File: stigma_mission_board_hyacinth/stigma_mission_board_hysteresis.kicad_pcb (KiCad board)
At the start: 4 copper layers, 70 x 110 mm, 269 parts, among them J10 Conn_02x05_Top_Bottom_Mountin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, J13 SMA, J16 Conn_02x02_Top_Bottom, J17 Conn_02x02_Top_Bottom, J18 Conn_02x02_Top_Bottom, J19 Conn_02x02_Top_Bottom, J2 SMA, J3 Conn_02x04_Top_Bottom, J5 Conn_02x02_Top_Bottom, J6 JST-GH, J8 Conn_02x04_Top_Bottom, Q1 DMN2056U, Q10 DMN2056U, Q11 AOSP21321, Q14 DMN2056U, Q15 AOSP21321, Q2 DMN2056U, Q3 AOSP21321, Q6 DMN2056U, Q7 AOSP21321, U1 L7805, U10 Ai-Thinker-Ra-01, U10 INA181, U11 INA181, U12 LAN8742A, U13 TPD4E1U06, U14 INA181, U16 INA181, U17 Ai-Thinker-Ra-01, U2 L7805, U3 Ai-Thinker-Ra-01, U3 L7805, U4 SN74HCS594, U5 MCP2562-E-SN, U6 MCP2562-E-SN, U7 AZ1117H-ADJ, U8 AZ1117H-ADJ, U9 INA181, Y1 25MHz

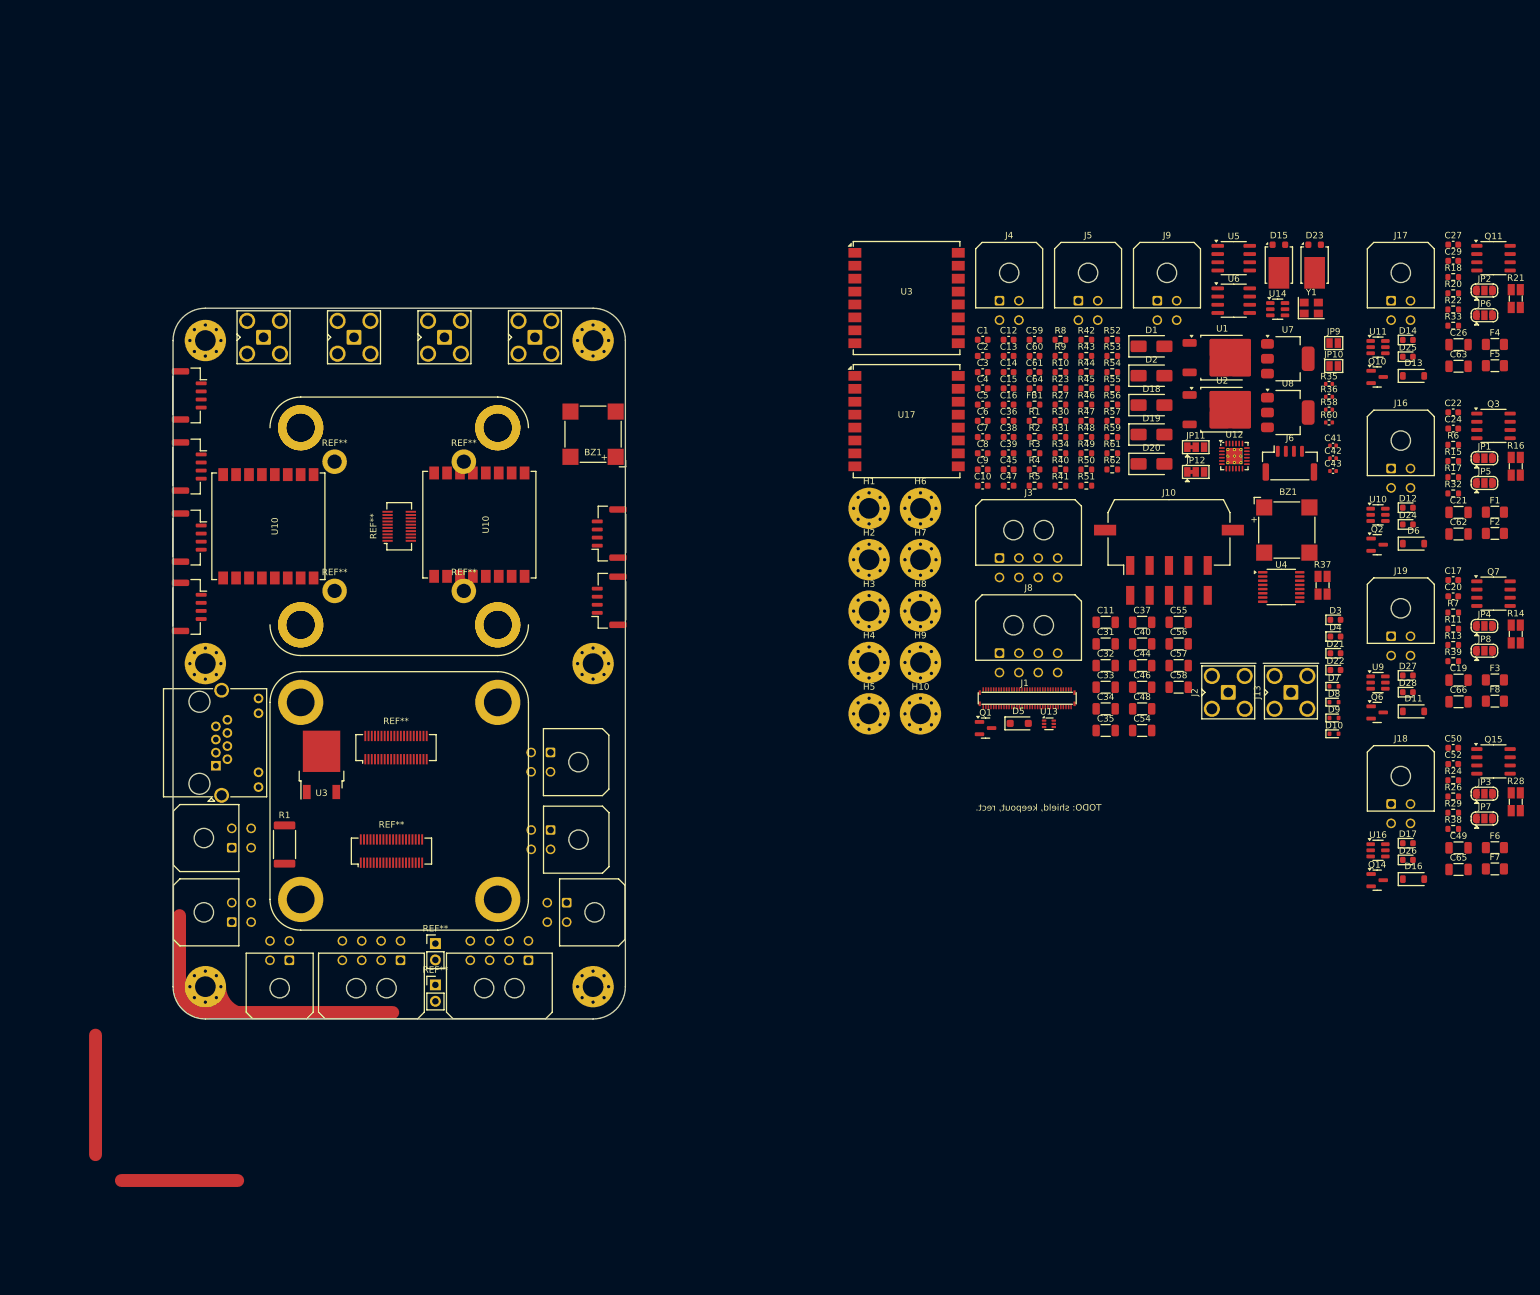
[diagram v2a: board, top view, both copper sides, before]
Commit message: changed pcb layout and added first tracks
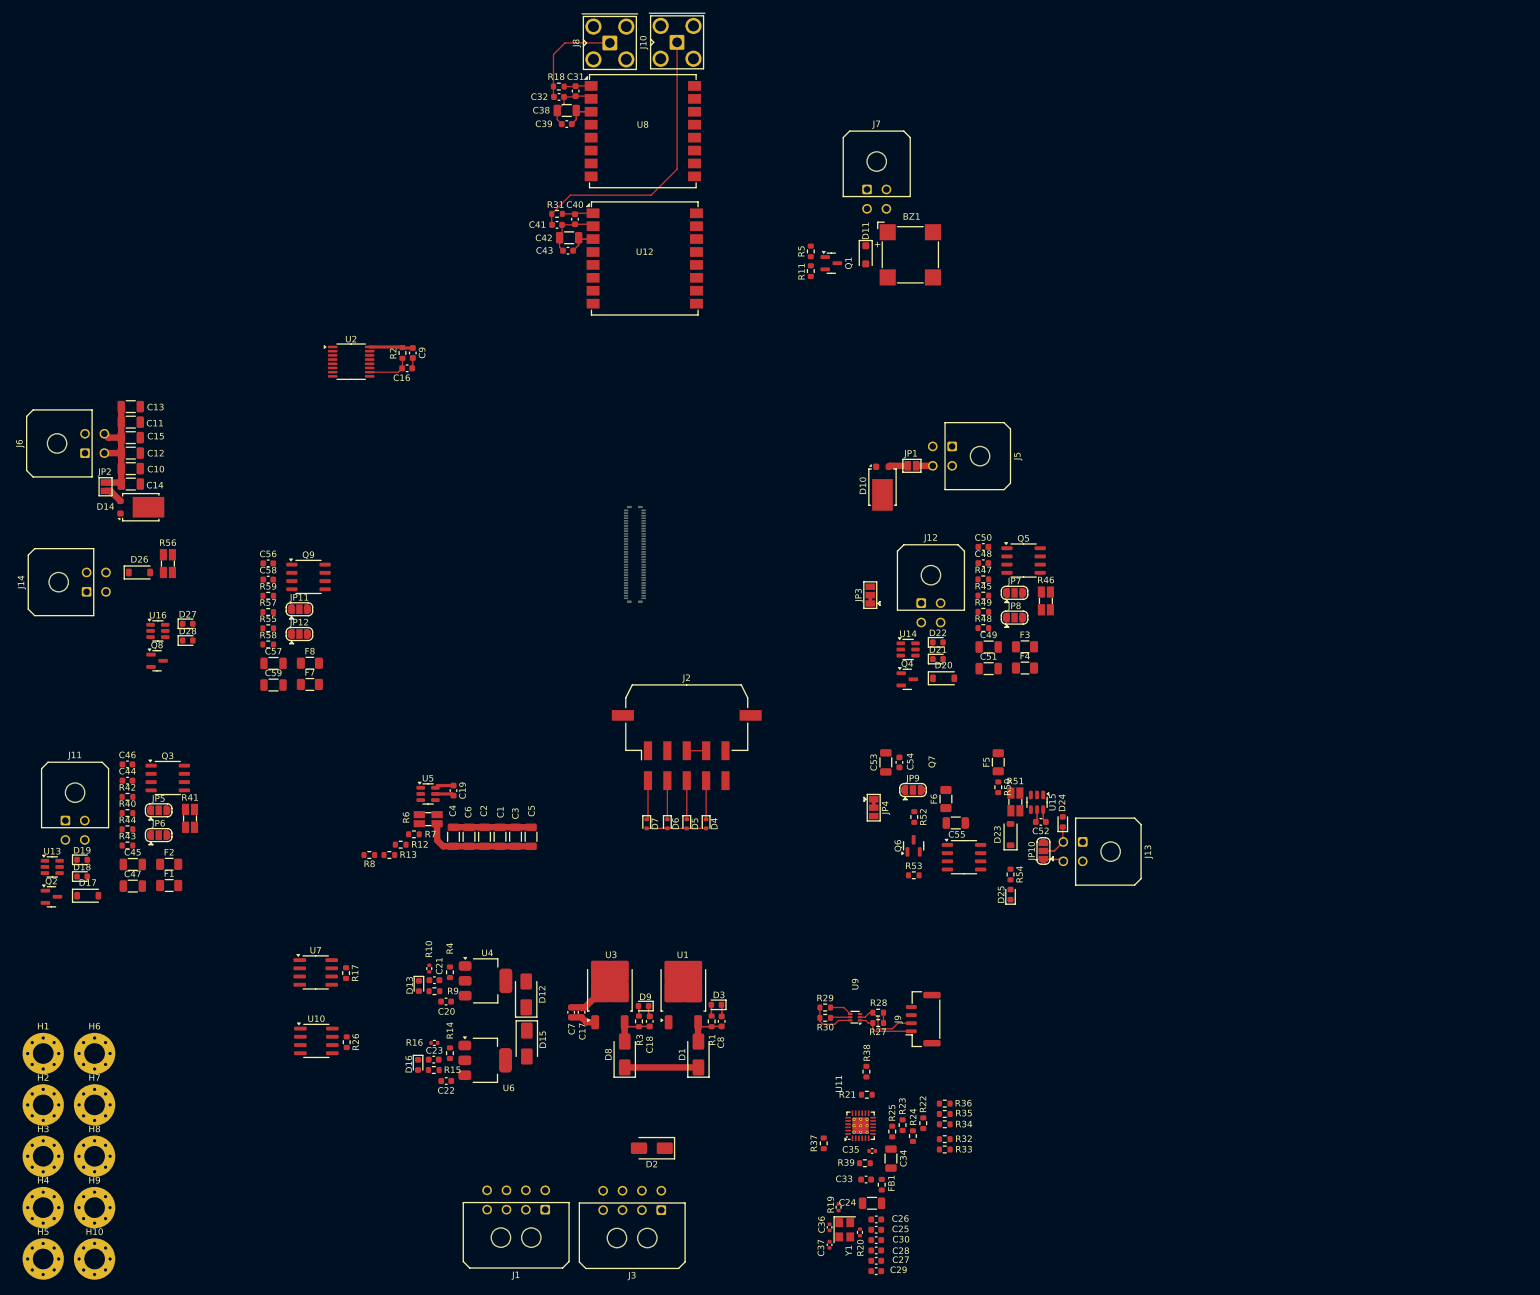
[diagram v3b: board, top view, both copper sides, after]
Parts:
- removed the BZ1 at (105.0, 64.5)
- removed the R1 at (57.2, 128.0)
- removed REF** (x2): Molex_Micro-Fit_3.0_43045-0800_2x04_P3.00mm_Horizontal, Connector_Molex:Molex_Micro-Fit_3.0_43045-0800_2x04_P3.00mm_Horizontal
- removed REF** (x12): MountingHole_4.3mm_M4_ISO14580_Pad, MountingHole:MountingHole_4.3mm_M4_ISO14580_Pad
- removed REF** (x4): SMA_Amphenol_901-143_Horizontal, Connector_Coaxial:SMA_Amphenol_901-143_Horizontal
- removed REF** (x6): JST_GH_SM04B-GHS-TB_1x04-1MP_P1.25mm_Horizontal, Connector_JST:JST_GH_SM04B-GHS-TB_1x04-1MP_P1.25mm_Horizontal
- removed REF** (x6): Molex_Micro-Fit_3.0_43045-0400_2x02_P3.00mm_Horizontal, Connector_Molex:Molex_Micro-Fit_3.0_43045-0400_2x02_P3.00mm_Horizontal
- removed REF** (x4): MountingHole_2.2mm_M2_ISO14580_Pad, MountingHole:MountingHole_2.2mm_M2_ISO14580_Pad
- removed REF** (x6): MountingHole_3.2mm_M3_Pad_Via, MountingHole:MountingHole_3.2mm_M3_Pad_Via
- removed REF**: RJ45_Amphenol_RJHSE538X, Connector_RJ:RJ45_Amphenol_RJHSE538X
- removed REF** (x2): PinHeader_1x02_P2.54mm_Vertical, Connector_PinHeader_2.54mm:PinHeader_1x02_P2.54mm_Vertical
- removed REF** (x2): Hirose_DF12_DF12E3.0-40DP-0.5V_2x20_P0.50mm_Vertical, Connector_Hirose:Hirose_DF12_DF12E3.0-40DP-0.5V_2x20_P0.50mm_Vertical
- removed REF**: Hirose_DF12_DF12C3.0-20DS-0.5V_2x10_P0.50mm_Vertical, Connector_Hirose:Hirose_DF12_DF12C3.0-20DS-0.5V_2x10_P0.50mm_Vertical
- removed the U10 at (54.8, 78.8)
- removed the U10 at (87.4, 78.5)
- removed the U3 at (63.0, 115.7)
- J4: renamed from J1; moved to B.Cu
- moved C44 212.3 mm to (32.9, 118.1)
- moved C45 212.3 mm to (33.8, 131.1)
- moved C46 212.3 mm to (32.9, 115.6)
- moved C47 212.3 mm to (33.8, 134.4)
- moved Q3 212.3 mm to (39.2, 117.7)
- moved R40 212.3 mm to (32.9, 123.1)
- moved R41 212.3 mm to (42.6, 124.0)
- moved R42 212.3 mm to (32.9, 120.6)
- moved R43 212.3 mm to (32.9, 128.2)
- moved R44 212.3 mm to (32.9, 125.6)
- moved D17 212.3 mm to (26.8, 135.9)
- moved D18 212.3 mm to (25.9, 133.0)
- moved D19 212.3 mm to (25.9, 130.4)
- moved F1 212.3 mm to (39.4, 134.3)
- moved F2 212.3 mm to (39.4, 131.1)
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- renumbered C31 to C1, C32 to C10, C34 to C11, C35 to C12, C54 to C13, C56 to C14, C58 to C15, C8 to C16, C2 to C17, C4 to C18, C47 to C19, C33 to C2, C12 to C20, C13 to C21, C14 to C22, C15 to C23, C37 to C24, C38 to C25, C39 to C26, C60 to C27, C61 to C28, C59 to C29, C46 to C3, C36 to C30, C5 to C31, C6 to C32, C64 to C33, C40 to C34, C41 to C35, C42 to C36, C43 to C37, C44 to C38, C45 to C39, C48 to C4, C9 to C40, C10 to C41, C11 to C42, C16 to C43, C24 to C44, C21 to C45, C22 to C46, C62 to C47, C29 to C48, C26 to C49, C55 to C5, C27 to C50, C63 to C51, C49 to C53, C50 to C54, C65 to C55, C17 to C56, C19 to C57, C20 to C58, C66 to C59, C57 to C6, C1 to C7, C3 to C8, C7 to C9, D15 to D10, D5 to D11, D2 to D12, D21 to D13, D23 to D14, D20 to D15, D22 to D16, D6 to D17, D24 to D18, D12 to D19, D19 to D2, D13 to D20, D25 to D21, D14 to D22, D16 to D23, D26 to D24, D17 to D25, D11 to D26, D7 to D4, D8 to D5, D9 to D6, D10 to D7, D18 to D8, D4 to D9, F2 to F1, F1 to F2, F4 to F3, F5 to F4, F6 to F5, F7 to F6, F8 to F7, F3 to F8, J8 to J1, J13 to J10, J16 to J11, J17 to J12, J18 to J13, J19 to J14, J10 to J2, J4 to J5, J9 to J6, J5 to J7, J2 to J8, J6 to J9, JP9 to JP1, JP7 to JP10, JP4 to JP11, JP8 to JP12, JP10 to JP2, JP12 to JP3, JP11 to JP4, JP1 to JP5, JP5 to JP6, JP2 to JP7, JP6 to JP8, JP3 to JP9, Q10 to Q4, Q11 to Q5, Q14 to Q6, Q15 to Q7, Q6 to Q8, Q7 to Q9, R60 to R10, R8 to R11, R27 to R12, R31 to R13, R57 to R14, R62 to R15, R58 to R16, R9 to R17, R3 to R18, R35 to R19, R4 to R2, R36 to R20, R55 to R21, R53 to R22, R48 to R23, R47 to R24, R46 to R25, R10 to R26, R41 to R27, R42 to R28, R43 to R29, R2 to R3, R44 to R30, R5 to R31, R45 to R32, R49 to R33, R50 to R34, R51 to R35, R52 to R36, R34 to R37, R54 to R38, R56 to R39, R59 to R4, R15 to R40, R16 to R41, R6 to R42, R32 to R43, R17 to R44, R20 to R45, R21 to R46, R18 to R47, R33 to R48, R22 to R49, R40 to R5, R26 to R50, R28 to R51, R24 to R52, R38 to R53, R29 to R54, R13 to R55, R14 to R56, R11 to R57, R39 to R58, R7 to R59, R37 to R6, R23 to R7, R30 to R8, R61 to R9, U6 to U10, U12 to U11, U17 to U12, U10 to U13, U11 to U14, U16 to U15, U9 to U16, U4 to U2, U2 to U3, U7 to U4, U14 to U5, U8 to U6, U5 to U7, U3 to U8, U13 to U9
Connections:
- J2 pad MP: unconnected-(J10-MountPin-PadMP) -> GND
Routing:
- net (no net): track 90.2 -> 0.00 mm
- net GND: track 0.00 -> 58.2 mm
- net Net-(J10-In): track 0.00 -> 43.6 mm
- net main_voltage: track 0.00 -> 21.5 mm
- net high_current: track 0.00 -> 20.0 mm
- net Net-(J8-In): track 0.00 -> 16.1 mm
- net +3.3V: track 0.00 -> 11.8 mm
- net +5V: track 0.00 -> 11.4 mm
- net /TXN: track 0.00 -> 10.5 mm
- net +3V3: track 0.00 -> 9.44 mm
- net /TXP: track 0.00 -> 9.19 mm
- net Net-(U11-VDD1A): track 0.00 -> 8.86 mm
- net Net-(U2-~{RCLR}): track 0.00 -> 6.84 mm
- net Net-(D1-A): track 0.00 -> 6.67 mm
- net Net-(D8-A): track 0.00 -> 6.60 mm
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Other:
- board outline removed
- board text added: "3.3V Regulator"
- board text added: "5V Regulator"
- board text added: "@TODO -wohin mit den Teilen, die rechts sind? -Brauchen wir auf dem Board echt Bezeichner + Value, oder reicht Bezeichner? -ist der Connector jetzt falsch rum, weil er blau ist? -Gibt es Teile, die näher am Connector sein MÜSSEN, bzw. bei welchen ist es weniger wichtig? - Über Paint (Bezeichner und so) kann man schon Vias verlegen, oder?"
- board text added: "Buzzer + DAC"
- board text added: "CAN"
- board text added: "Ethernet"
- board text added: "GPS"
- board text added: "LoRa Module"
- board text added: "R1"
- board text added: "R2"
- board text added: "R3"
- board text added: "R4"
- board text added: "Recovery Power 1"
- board text added: "Recovery Power 2"
- board text added: "Shift Register IO"
- board text added: "Vehicle BUS"
- board text added: "Voltage & Current Sensing"

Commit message: placed recovery outputs and vehicle bus, fixed errors in schematic
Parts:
- removed J9: JST-GH, Connector_JST:JST_GH_SM04B-GHS-TB_1x04-1MP_P1.25mm_Horizontal
- added R60: 270, Resistor_SMD:R_0603_1608Metric, F.Cu at (169.1, 181.8)
- added R61: 10k, Resistor_SMD:R_0603_1608Metric, F.Cu at (169.1, 184.3)
- added R62: 270, Resistor_SMD:R_0603_1608Metric, F.Cu at (169.1, 186.8)
- added RJ45: ~, Stigma:RJ45-TH_MJ88B-B011-RVL11-P, F.Cu at (157.9, 183.0)
- D10, D14: value SVT12100 -> SS34; footprint Package_TO_SOT_SMD:TO-277B -> Diode_SMD:D_SMA
- J2, U1, U12, U3, U4, U6, U8: moved to B.Cu
- JP3, JP4: value SolderJumper_3_Bridged12 -> servo_switch; footprint Jumper:SolderJumper-3_P1.3mm_Bridged12_Pad1.0x1.5mm -> Jumper:SolderJumper-3_P1.3mm_Open_RoundedPad1.0x1.5mm
- moved H6 393.0 mm to (396.3, 23.7)
- moved H10 369.1 mm to (396.2, 216.2)
- moved H1 360.7 mm to (353.7, 23.6)
- moved H5 334.8 mm to (353.8, 216.2)
- moved R18 279.7 mm to (378.0, 38.6)
- moved C39 279.6 mm to (379.1, 44.8)
- moved R31 279.6 mm to (377.7, 56.9)
- moved C31 279.6 mm to (380.4, 39.4)
- moved C38 279.4 mm to (378.9, 42.6)
- moved C40 279.3 mm to (380.2, 57.5)
- moved C43 279.0 mm to (378.9, 62.8)
- moved C42 278.6 mm to (378.7, 60.6)
- moved C32 277.3 mm to (375.6, 39.4), turned to 90 degrees
- moved C41 277.0 mm to (375.2, 57.6), turned to 90 degrees
- moved J1 274.5 mm to (370.9, 210.4)
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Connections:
- net ETH_LED_2 renamed ETH_nINT
- C38 pad 2: +3V3 -> +3.3V
- C39 pad 2: +3V3 -> +3.3V
- C42 pad 2: +3V3 -> +3.3V
- C43 pad 2: +3V3 -> +3.3V
- C45 pad 2: +3V3 -> +3.3V
- C46 pad 2: +3V3 -> +3.3V
- C49 pad 2: +3V3 -> +3.3V
- C50 pad 2: +3V3 -> +3.3V
- C53 pad 2: +3V3 -> +3.3V
- C54 pad 2: +3V3 -> +3.3V
- C57 pad 2: +3V3 -> +3.3V
- C58 pad 2: +3V3 -> +3.3V
- U11 pad 3: ETH_LED_1 -> Net-(RJ45-L+)
- U12 pad 3: +3V3 -> +3.3V
- U8 pad 3: +3V3 -> +3.3V
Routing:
- net Net-(J10-In): track 43.6 -> 0.00 mm
- net RECOVERY_4_CONT_CHECK: track 0.00 -> 26.4 mm
- net +3.3V: track 11.8 -> 36.5 mm
- net RECOVERY_2_CONT_CHECK: track 0.00 -> 23.2 mm
- net Net-(D23-K): track 3.20 -> 24.5 mm
- net high_current_2: track 0.00 -> 20.4 mm
- net GND: track 58.2 -> 78.5 mm, vias 0 -> 14
- net Net-(D20-K): track 0.00 -> 20.0 mm
- net +5V: track 11.4 -> 29.1 mm
- net Net-(J8-In): track 16.1 -> 0.00 mm
- net Net-(Q6-D): track 0.00 -> 14.5 mm
- net ADC_RECOVERY_4_I: track 0.00 -> 13.4 mm
- net Net-(D21-K): track 0.00 -> 11.9 mm
- net Net-(C55-Pad1): track 0.00 -> 11.4 mm
- net RECOVERY_4: track 0.00 -> 11.4 mm
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- added copper zone on In1.Cu, net GND
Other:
- board outline added: 50 x 200 mm
- board text added: "50 x 200 mm"
- board text removed: "@TODO -wohin mit den Teilen, die rechts sind? -Brauchen wir auf dem Board echt Bezeichner + Value, oder reicht Bezeichner? -ist der Connector jetzt falsch rum, weil er blau ist? -Gibt es Teile, die näher am Connector sein MÜSSEN, bzw. bei welchen ist es weniger wichtig? - Über Paint (Bezeichner und so) kann man schon Vias verlegen, oder?"

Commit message: made board more compact, started routing recovery outputs
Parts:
- removed C52, C54, C56, C58: 100n, Capacitor_SMD:C_0603_1608Metric
- removed C53, C55, C57, C59: 10u, Capacitor_SMD:C_1206_3216Metric
- removed J14: Conn_02x02_Top_Bottom, Connector_Molex:Molex_Micro-Fit_3.0_43045-0400_2x02_P3.00mm_Horizontal
- removed JP10, JP11, JP12, JP7, JP8, JP9: servo_switch, Jumper:SolderJumper-3_P1.3mm_Open_RoundedPad1.0x1.5mm
- removed R59: 1k, Resistor_SMD:R_0603_1608Metric
- removed R60, R62: 270, Resistor_SMD:R_0603_1608Metric
- removed R61: 10k, Resistor_SMD:R_0603_1608Metric
- removed RJ45: ~, Stigma:RJ45-TH_MJ88B-B011-RVL11-P
- added J9: SMA, Connector_Coaxial:SMA_Amphenol_901-143_Horizontal, F.Cu at (235.0, 104.5)
- added RJ1: ~, stigma:RJ45-TH_MJ88B-B011-RVL11-P, F.Cu at (238.0, 143.0)
- added Shunt1: 250mR 1%, Resistor_SMD:R_0805_2012Metric, F.Cu at (274.0, 153.8)
- added Shunt2: 250mR 1%, Resistor_SMD:R_0805_2012Metric, F.Cu at (229.0, 201.5)
- added Shunt3: 250mR 1%, Resistor_SMD:R_0805_2012Metric, F.Cu at (229.0, 222.1)
- added Shunt4: 250mR 1%, Resistor_SMD:R_0805_2012Metric, F.Cu at (281.6, 148.5)
- C31, C32: value DNP -> 10p; footprint Capacitor_SMD:C_0603_1608Metric -> Capacitor_SMD:C_0402_1005Metric
- C33: value 100n -> DNP
- C34: value 1u -> DNP; footprint Capacitor_SMD:C_1206_3216Metric -> Capacitor_SMD:C_0603_1608Metric
- C35: value 470p -> 100n; footprint Capacitor_SMD:C_0402_1005Metric -> Capacitor_SMD:C_0603_1608Metric
- C36: value 10p -> 1u; footprint Capacitor_SMD:C_0402_1005Metric -> Capacitor_SMD:C_1206_3216Metric
- C37: value 10p -> 470p
- F1, F5: value 100mA -> 10A
- F3, F7: value 100mA -> 10A; moved to B.Cu
- F4, F8: moved to B.Cu
- J10: value SMA -> Conn_02x02_Top_Bottom; footprint Connector_Coaxial:SMA_Amphenol_901-143_Horizontal -> Connector_Molex:Molex_Micro-Fit_3.0_43045-0400_2x02_P3.00mm_Horizontal
- J2: footprint Connector_Molex:Molex_Micro-Fit_3.0_43045-1010_2x05-1MP_P3.00mm_Horizontal -> stigma:DF40GB-10DP-0.4V-plug
- J7: value Conn_02x02_Top_Bottom -> JST-GH 4Pin; footprint Connector_Molex:Molex_Micro-Fit_3.0_43045-0400_2x02_P3.00mm_Horizontal -> Connector_JST:JST_GH_BM04B-GHS-TBT_1x04-1MP_P1.25mm_Vertical
- JP3, JP4, JP5, JP6: footprint Jumper:SolderJumper-3_P1.3mm_Open_RoundedPad1.0x1.5mm -> Jumper:SolderJumper-3_Open_RoundedPad2x2mm
- R17: value 120, DNP -> 0; footprint Resistor_SMD:R_0603_1608Metric -> Resistor_SMD:R_0402_1005Metric
- R18: footprint Resistor_SMD:R_0603_1608Metric -> Resistor_SMD:R_0402_1005Metric
- R19: value 0 -> 120, DNP; footprint Resistor_SMD:R_0402_1005Metric -> Resistor_SMD:R_0603_1608Metric
- R20: footprint Resistor_SMD:R_0402_1005Metric -> Resistor_SMD:R_0603_1608Metric
- R40: value 60R -> 270
- R41: value 100mR 1% -> 270; footprint Resistor_SMD:R_Shunt_Ohmite_LVK12 -> Resistor_SMD:R_0603_1608Metric
- R42, R49, R57: value 1k -> 10k
- R43: value 10k -> 60R
- R45: value 60R -> 10k
- R46, R56: value 100mR 1% -> 1k; footprint Resistor_SMD:R_Shunt_Ohmite_LVK12 -> Resistor_SMD:R_0603_1608Metric
- R47: value 1k -> 60R
- R48, R58: value 10k -> 1k
- R50: value 60R -> 1k
- R51: value 100mR 1% -> 60R; footprint Resistor_SMD:R_Shunt_Ohmite_LVK12 -> Resistor_SMD:R_0603_1608Metric
- moved C51 279.2 mm to (111.2, 193.2), turned to 180 degrees
- moved J10 240.9 mm to (209.6, 203.0), turned to 90 degrees
- moved C45 234.8 mm to (264.9, 172.7)
- moved J11 229.9 mm to (240.4, 200.1), turned to -90 degrees
- moved D10 225.2 mm to (163.6, 60.2)
- moved F5 225.2 mm to (172.6, 118.4)
- moved JP1 225.2 mm to (167.2, 62.4)
- moved JP3 225.2 mm to (158.6, 68.6)
- moved R45 225.2 mm to (171.4, 89.9)
- moved F6 225.2 mm to (163.5, 105.5)
- moved R46 225.2 mm to (168.3, 88.2)
- moved JP5 220.3 mm to (234.9, 220.9), turned to 90 degrees
- moved J6 217.4 mm to (209.6, 184.5)
- moved C46 212.4 mm to (229.5, 196.0)
- moved C47 208.1 mm to (229.0, 206.5), turned to 180 degrees
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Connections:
- BZ1 pad 3: (no net) -> unconnected-(BZ1-Pad3)
- BZ1 pad 4: (no net) -> unconnected-(BZ1-Pad4)
- C31 pad 2: Net-(U8-ANT) -> Net-(C31-Pad2)
- C32 pad 2: Net-(J8-In) -> Net-(C32-Pad2)
- C33 pad 1: +3.3V -> GND
- C33 pad 2: GND -> Net-(U8-ANT)
- C34 pad 1: Net-(U11-VDDCR) -> GND
- C34 pad 2: GND -> Net-(J8-In)
- C35 pad 1: Net-(U11-VDDCR) -> +3.3V
- C36 pad 1: GND -> Net-(U11-VDDCR)
- C36 pad 2: Net-(C36-Pad2) -> GND
- C37 pad 1: GND -> Net-(U11-VDDCR)
- C37 pad 2: Net-(C37-Pad2) -> GND
- C41 pad 2: Net-(J10-In) -> Net-(J9-In)
- C45 pad 1: GND -> /Recovery Output3/high_current
- C45 pad 2: +3.3V -> GND
- C46 pad 1: GND -> +3.3V
- C46 pad 2: +3.3V -> GND
- C47 pad 1: Net-(C47-Pad1) -> /Recovery Output2/high_current
- C49 pad 1: GND -> /Recovery Output 4/high_current
- C49 pad 2: +3.3V -> GND
- C50 pad 1: GND -> +3.3V
- C50 pad 2: +3.3V -> GND
- C51 pad 1: Net-(C51-Pad1) -> /Recovery Output 1/high_current
- D17 pad 1: Net-(D17-K) -> /Recovery Output3/recovery_switched
- D18 pad 1: Net-(D18-K) -> /Recovery Output3/servo_line
- D20 pad 1: Net-(D20-K) -> /Recovery Output2/recovery_switched
- D21 pad 1: Net-(D21-K) -> /Recovery Output2/servo_line
- D23 pad 1: Net-(D23-K) -> /Recovery Output 4/recovery_switched
- D24 pad 1: Net-(D24-K) -> /Recovery Output 4/servo_line
- D26 pad 1: Net-(D26-K) -> /Recovery Output 1/recovery_switched
- D27 pad 1: Net-(D27-K) -> /Recovery Output 1/servo_line
- F1 pad 1: Net-(F1-Pad1) -> /Recovery Output 1/high_current
- F1 pad 2: RECOVERY_3_CONT_CHECK -> high_current
- F2 pad 1: Net-(C47-Pad1) -> /Recovery Output 1/high_current
- F2 pad 2: Net-(JP5-C) -> +5V
- F3 pad 1: Net-(F3-Pad1) -> /Recovery Output2/high_current
- F3 pad 2: RECOVERY_2_CONT_CHECK -> high_current
- F4 pad 1: Net-(C51-Pad1) -> high_current_2
- F4 pad 2: Net-(JP7-C) -> /Recovery Output2/high_current
- F5 pad 1: Net-(F5-Pad1) -> /Recovery Output3/high_current
- F5 pad 2: RECOVERY_4_CONT_CHECK -> high_current
- F6 pad 1: Net-(C55-Pad1) -> /Recovery Output3/high_current
- F6 pad 2: Net-(JP9-C) -> +5V
- F7 pad 1: Net-(F7-Pad1) -> /Recovery Output 4/high_current
- F7 pad 2: RECOVERY_1_CONT_CHECK -> high_current
- F8 pad 1: Net-(C59-Pad1) -> high_current_2
- F8 pad 2: Net-(JP11-C) -> /Recovery Output 4/high_current
- J10 pad 1: Net-(J10-In) -> GND
- J11 pad 3: Net-(D18-K) -> /Recovery Output2/servo_line
- J11 pad 4: Net-(D17-K) -> /Recovery Output2/recovery_switched
- J12 pad 3: Net-(D21-K) -> /Recovery Output 4/servo_line
- J12 pad 4: Net-(D20-K) -> /Recovery Output 4/recovery_switched
- J13 pad 3: Net-(D24-K) -> /Recovery Output 1/servo_line
- J13 pad 4: Net-(D23-K) -> /Recovery Output 1/recovery_switched
- J7 pad 1: GND -> +5V
- J7 pad 2: GND -> DAC
- J7 pad 3: DAC -> GND
- J7 pad 4: +5V -> GND
- JP3 pad 1: high_current_2 -> /Recovery Output3/recovery_switched
- JP3 pad 2: /Recovery Output2/high_current -> /Recovery Output3/servo_line
- JP3 pad 3: high_current -> /Recovery Output3/high_current
- JP4 pad 1: high_current_2 -> /Recovery Output2/recovery_switched
- JP4 pad 2: /Recovery Output 4/high_current -> /Recovery Output2/servo_line
- JP4 pad 3: high_current -> /Recovery Output2/high_current
- JP5 pad 1: high_current -> /Recovery Output 4/recovery_switched
- JP5 pad 2: Net-(JP5-C) -> /Recovery Output 4/servo_line
- JP5 pad 3: +5V -> /Recovery Output 4/high_current
- JP6 pad 1: Net-(D17-K) -> /Recovery Output 1/recovery_switched
- JP6 pad 2: Net-(D18-K) -> /Recovery Output 1/servo_line
- JP6 pad 3: high_current -> /Recovery Output 1/high_current
- Q3 pad 1: Net-(C47-Pad1) -> /Recovery Output3/high_current
- Q3 pad 2: Net-(C47-Pad1) -> /Recovery Output3/high_current
- Q3 pad 3: Net-(C47-Pad1) -> /Recovery Output3/high_current
- Q3 pad 5: Net-(D17-K) -> /Recovery Output3/recovery_switched
- Q3 pad 6: Net-(D17-K) -> /Recovery Output3/recovery_switched
- Q3 pad 7: Net-(D17-K) -> /Recovery Output3/recovery_switched
- Q3 pad 8: Net-(D17-K) -> /Recovery Output3/recovery_switched
- Q5 pad 1: Net-(C51-Pad1) -> /Recovery Output2/high_current
- Q5 pad 2: Net-(C51-Pad1) -> /Recovery Output2/high_current
- Q5 pad 3: Net-(C51-Pad1) -> /Recovery Output2/high_current
- Q5 pad 5: Net-(D20-K) -> /Recovery Output2/recovery_switched
- Q5 pad 6: Net-(D20-K) -> /Recovery Output2/recovery_switched
- Q5 pad 7: Net-(D20-K) -> /Recovery Output2/recovery_switched
- Q5 pad 8: Net-(D20-K) -> /Recovery Output2/recovery_switched
- Q7 pad 1: Net-(C55-Pad1) -> /Recovery Output 4/high_current
- Q7 pad 2: Net-(C55-Pad1) -> /Recovery Output 4/high_current
- Q7 pad 3: Net-(C55-Pad1) -> /Recovery Output 4/high_current
- Q7 pad 5: Net-(D23-K) -> /Recovery Output 4/recovery_switched
- Q7 pad 6: Net-(D23-K) -> /Recovery Output 4/recovery_switched
- Q7 pad 7: Net-(D23-K) -> /Recovery Output 4/recovery_switched
- Q7 pad 8: Net-(D23-K) -> /Recovery Output 4/recovery_switched
- Q9 pad 1: Net-(C59-Pad1) -> /Recovery Output 1/high_current
- Q9 pad 2: Net-(C59-Pad1) -> /Recovery Output 1/high_current
- Q9 pad 3: Net-(C59-Pad1) -> /Recovery Output 1/high_current
- Q9 pad 5: Net-(D26-K) -> /Recovery Output 1/recovery_switched
- Q9 pad 6: Net-(D26-K) -> /Recovery Output 1/recovery_switched
- Q9 pad 7: Net-(D26-K) -> /Recovery Output 1/recovery_switched
- Q9 pad 8: Net-(D26-K) -> /Recovery Output 1/recovery_switched
- R17 pad 1: CAN_1_H -> HSE_IN
- R17 pad 2: CAN_1_L -> Net-(C31-Pad2)
- R18 pad 1: Net-(U8-ANT) -> Net-(C32-Pad2)
- R18 pad 2: Net-(J8-In) -> HSE_OUT
- R19 pad 1: HSE_IN -> CAN_1_H
- R19 pad 2: Net-(C36-Pad2) -> CAN_1_L
- R20 pad 1: Net-(C37-Pad2) -> Net-(U8-ANT)
- R20 pad 2: HSE_OUT -> Net-(J8-In)
- R31 pad 2: Net-(J10-In) -> Net-(J9-In)
- R39 pad 1: +3.3V -> ETH_nINT
- R39 pad 2: ETH_nINT -> GND
- R40 pad 1: Net-(F1-Pad1) -> Net-(RJ1-L-)
- R40 pad 2: Net-(R40-Pad2) -> GND
- R41 pad 1: Net-(R40-Pad2) -> Net-(RJ1-R+)
- R41 pad 2: Net-(U13-+) -> GND
- R42 pad 1: Net-(JP5-C) -> +3.3V
- R42 pad 2: Net-(Q2-D) -> ETH_nINT
- R43 pad 1: RECOVERY_3 -> RECOVERY_3_CONT_CHECK
- R43 pad 2: GND -> Net-(U13-+)
- R44 pad 1: Net-(D17-K) -> /Recovery Output3/high_current
- R44 pad 2: Net-(D19-A) -> Net-(Q2-D)
- R45 pad 1: Net-(F3-Pad1) -> RECOVERY_3
- R45 pad 2: Net-(R45-Pad2) -> GND
- R46 pad 1: Net-(R45-Pad2) -> /Recovery Output3/recovery_switched
- R46 pad 2: Net-(U14-+) -> Net-(D19-A)
- R47 pad 1: Net-(JP7-C) -> RECOVERY_2_CONT_CHECK
- R47 pad 2: Net-(Q4-D) -> Net-(U14-+)
- R48 pad 1: RECOVERY_2 -> /Recovery Output2/high_current
- R48 pad 2: GND -> Net-(Q4-D)
- R49 pad 1: Net-(D20-K) -> RECOVERY_2
- R49 pad 2: Net-(D22-A) -> GND
- R50 pad 1: Net-(F5-Pad1) -> /Recovery Output2/recovery_switched
- R50 pad 2: Net-(R50-Pad2) -> Net-(D22-A)
- R51 pad 1: Net-(R50-Pad2) -> RECOVERY_4_CONT_CHECK
- R52 pad 1: Net-(JP9-C) -> /Recovery Output 4/high_current
- R54 pad 1: Net-(D23-K) -> /Recovery Output 4/recovery_switched
- R55 pad 1: Net-(F7-Pad1) -> RECOVERY_1_CONT_CHECK
- R55 pad 2: Net-(R55-Pad2) -> Net-(U16-+)
- R56 pad 1: Net-(R55-Pad2) -> /Recovery Output 1/high_current
- R56 pad 2: Net-(U16-+) -> Net-(Q8-D)
- R57 pad 1: Net-(JP11-C) -> RECOVERY_1
- R57 pad 2: Net-(Q8-D) -> GND
- R58 pad 1: RECOVERY_1 -> /Recovery Output 1/recovery_switched
- R58 pad 2: GND -> Net-(D28-A)
- U13 pad 4: Net-(U13--) -> Net-(D17-A)
- U14 pad 4: Net-(U14--) -> Net-(D20-A)
- U15 pad 4: Net-(U15--) -> Net-(D23-A)
- U16 pad 4: Net-(U16--) -> Net-(D26-A)
- Y1 pad 1: Net-(C36-Pad2) -> Net-(C31-Pad2)
- Y1 pad 3: Net-(C37-Pad2) -> Net-(C32-Pad2)
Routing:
- net GND: track 78.5 -> 19.2 mm, vias 14 -> 24
- net +3.3V: track 36.5 -> 1.56 mm
- net high_current: track 30.9 -> 0.00 mm
- net +5V: track 29.1 -> 0.00 mm
- net RECOVERY_4_CONT_CHECK: track 26.4 -> 0.00 mm
- net Net-(D23-K): track 24.5 -> 0.00 mm
- net RECOVERY_2_CONT_CHECK: track 23.2 -> 0.00 mm
- net main_voltage: track 21.5 -> 0.00 mm
- net high_current_2: track 20.4 -> 0.00 mm
- net Net-(D20-K): track 20.0 -> 0.00 mm
- net Net-(D24-K): track 15.4 -> 0.00 mm
- net Net-(Q6-D): track 14.5 -> 0.00 mm
- net ADC_RECOVERY_4_I: track 13.4 -> 0.00 mm
- net Net-(D21-K): track 11.9 -> 0.00 mm
- net Net-(C55-Pad1): track 11.4 -> 0.00 mm
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- added copper zone on B.Cu, net /Recovery Output 4/high_current
- added copper zone on F.Cu, net /Recovery Output 4/high_current
- added copper zone on F.Cu, net /Recovery Output 4/recovery_switched
- added copper zone on F.Cu, net /Recovery Output 4/servo_line
- added copper zone on F.Cu, net GND
- added copper zone on In2.Cu, net GND
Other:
- board size 50 x 200 mm -> 50 x 150 mm
